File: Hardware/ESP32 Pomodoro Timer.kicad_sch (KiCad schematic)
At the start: 6 parts, among them SW1 Start/Stop, SW2 RESET, SW3 Set Time, U1 ESP32-WROVER-E, U2 RC1602A

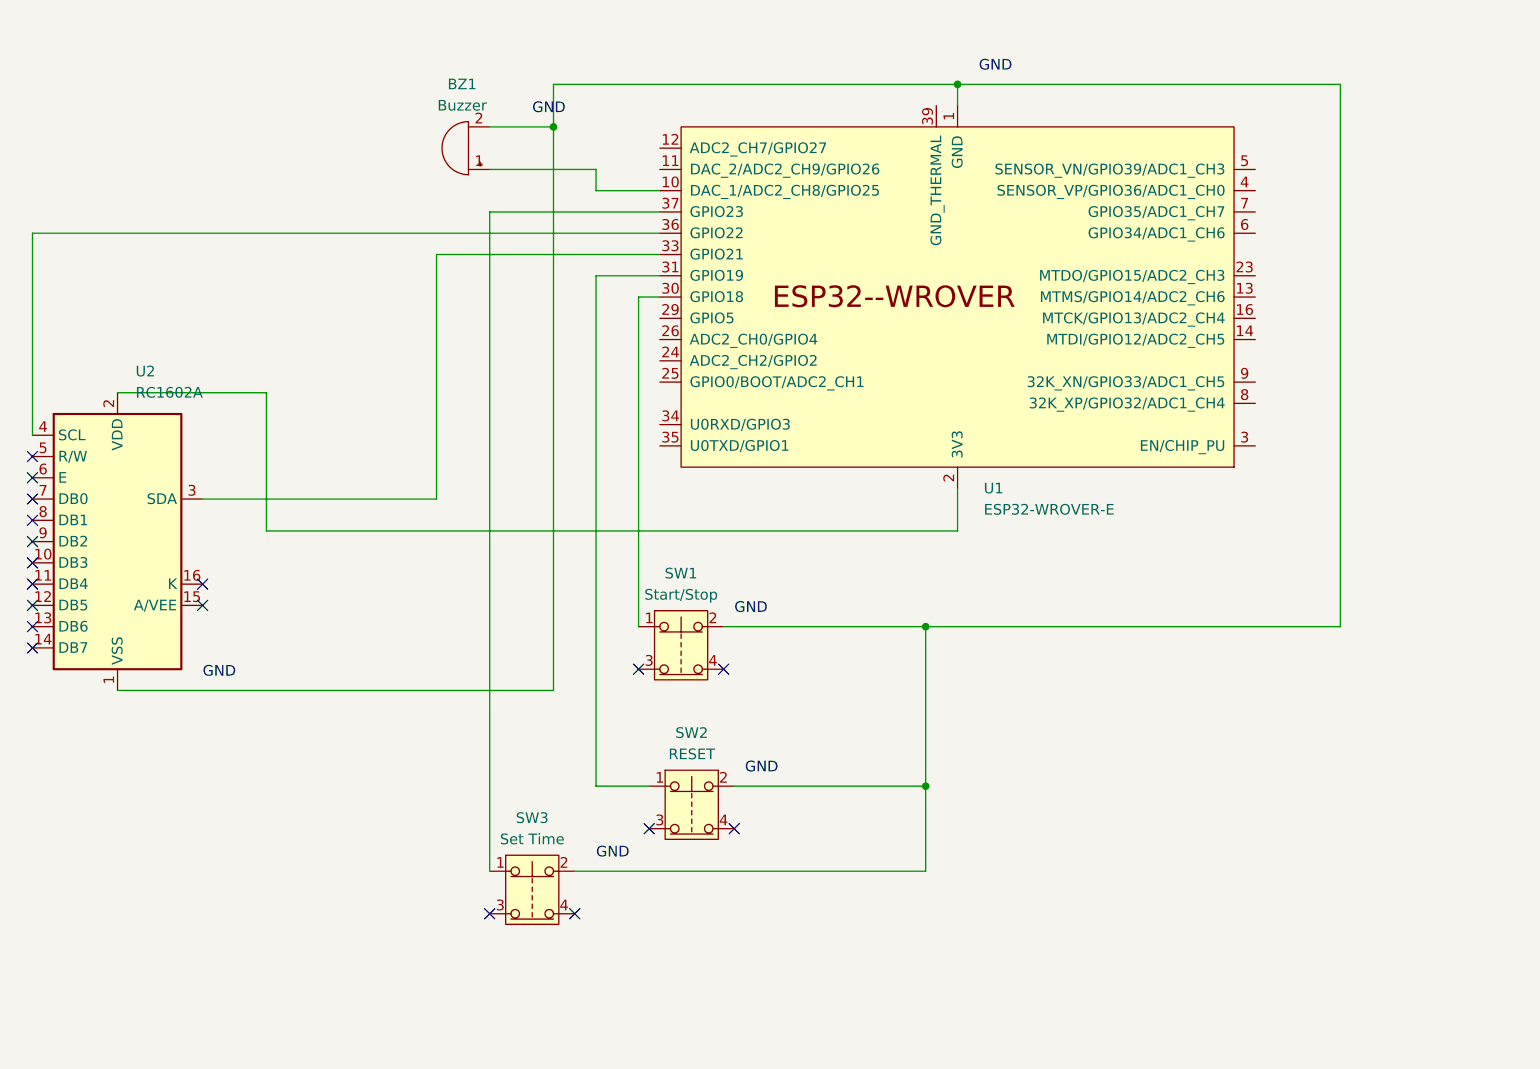
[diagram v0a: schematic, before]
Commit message: Add Wokwi simulation files for ESP32 Pomodoro Timer
- Created diagram.json to define the circuit layout including ESP32, LCD, buttons, and buzzer.
- Added wokwi.toml for project configuration and firmware paths.
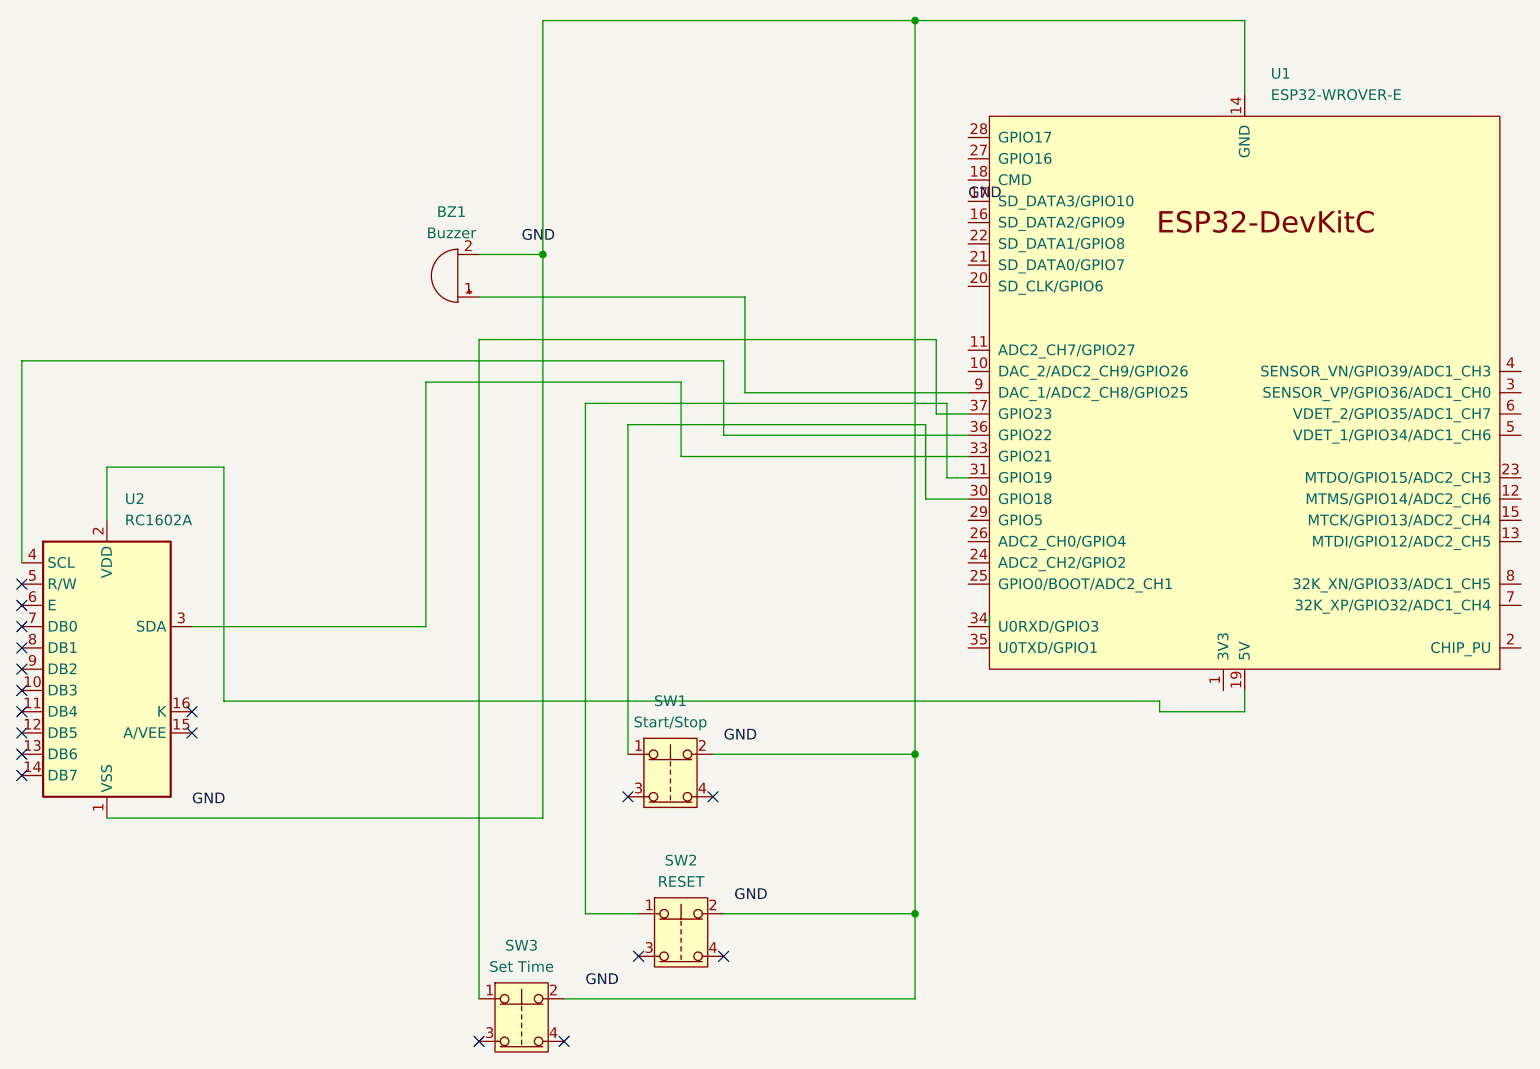
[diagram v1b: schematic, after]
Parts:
- U1: footprint PCM_Espressif:ESP32-WROVER-E -> PCM_Espressif:ESP32-DevKitC; symbol PCM_Espressif:ESP32-WROVER-E -> PCM_Espressif:ESP32-DevKitC
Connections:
- net GND: now also U1.17 (SD_DATA3/GPIO10)
- net at BZ1.2 (-), SW1.2, SW2.2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: now also U1.14 (GND), U1.32 (GND); no longer U1.1 (GND), U1.15 (GND)
- net at U2.2 (VDD): now also U1.19 (5V); no longer U1.2 (3V3)
- net at U1.10 (DAC_2/ADC2_CH9/GPIO26): no longer BZ1.1 (+)
- net at U1.9 (DAC_1/ADC2_CH8/GPIO25): now also BZ1.1 (+)
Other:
- moved on the sheet: BZ1, SW1, SW2, SW3, U2
